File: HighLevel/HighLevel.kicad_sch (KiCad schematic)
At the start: 28 parts, among them J10 Conn_01x06, J4 USB_A, J5 CAN, J6 SERVO, J7 AUX, J8 SWD, J9 COMM, Q1 MOFSET_N, SW1 SW_SPDT, U6 NRF24L01_Breakout

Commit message: Final High Level + edits + footprint
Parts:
- added C1: 2.2u, Capacitor_SMD:C_0805_2012Metric, symbol Device:C_Small
- C2: renamed from C20; footprint (none) -> Capacitor_SMD:C_0805_2012Metric
- C3: renamed from C21; footprint (none) -> Capacitor_SMD:C_0805_2012Metric
- D2: renamed from D3; footprint (none) -> LED_SMD:LED_0805_2012Metric
- D3: renamed from D2; footprint (none) -> LED_SMD:LED_0805_2012Metric
- D4: renamed from D1; footprint (none) -> LED_SMD:LED_0805_2012Metric
- R1: renamed from R27; footprint (none) -> Resistor_SMD:R_0805_2012Metric
- R10: renamed from R15; footprint (none) -> Resistor_SMD:R_0805_2012Metric
- R11: renamed from R13; footprint (none) -> Resistor_SMD:R_0805_2012Metric
- R12: renamed from R14; footprint (none) -> Resistor_SMD:R_0805_2012Metric
- R2: renamed from R28; footprint (none) -> Resistor_SMD:R_0805_2012Metric
- R3: renamed from R29; footprint (none) -> Resistor_SMD:R_0805_2012Metric
- R4: renamed from R24; footprint (none) -> Resistor_SMD:R_0805_2012Metric
- R5: renamed from R25; footprint (none) -> Resistor_SMD:R_0805_2012Metric
- R6: renamed from R16; footprint (none) -> Resistor_SMD:R_0805_2012Metric
- R7: renamed from R20; footprint (none) -> Resistor_SMD:R_0805_2012Metric
- R8: renamed from R23; footprint (none) -> Resistor_SMD:R_0805_2012Metric
- R9: renamed from R26; footprint (none) -> Resistor_SMD:R_0805_2012Metric
- SW1: footprint (none) -> Resistor_SMD:R_0805_2012Metric
- renumbered D4 to D1, J4 to J1, J10 to J2, J9 to J3, J6 to J4, J8 to J6, U6 to U1
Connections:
- net GND: now also U1.1 (GND), C1.1
- net VCC: now also U1.2 (VCC)
- net mcu/HALL_3: now also R1.1
- net mcu/PC10_UART_TX: now also U1.7 (MISO)
- net mcu/PX11_UART_RX: now also U1.5 (SCK)
- net mcu/TX_SCK_MOSI: now also U1.6 (MOSI)
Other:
- sheet driver ports: added HI1, HI2, HI3, HO1, HO2, HO3, HS1, HS2, HS3, LI1, LI2, LI3, LO1, LO2, LO3, SENS_1, SENS_2, SENS_3, SENS_FILTER, SENS_SUPPLY; removed none
- sheet power ports: added GH_A, GH_B, GH_C, GL_A, GL_B, GL_C, SH_A, SH_B, SH_C; removed none
- moved on the sheet: U1

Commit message: Fix all errors
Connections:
- net VCC: now also C1.2
- net mcu/SPI3_CE: now reaches U1.3 (CE)
- net mcu/SPI3_CSN: now reaches U1.4 (~{CSN})
- net mcu/PC10_UART_TX renamed mcu/SPI3_MISO
- net mcu/PC12 renamed mcu/PC13
- net mcu/PX11_UART_RX renamed mcu/SPI3_SCK
- net mcu/TX_SCK_MOSI renamed mcu/SPI3_MOSI
- no-connect marks 0 -> 1
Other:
- sheet mcu ports: added PC13, SPI3_CE, SPI3_CSN, SPI3_MISO, SPI3_MOSI, SPI3_SCK; removed PC10_UART_TX, PC12, PX11_UART_RX, TX_SCK_MOSI
- moved on the sheet: D1, J7, Q1, R4

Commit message: Started PCB and added connections to MCU
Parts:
- J1: footprint (none) -> Connector_USB:USB_Micro-B_Molex-105017-0001
- J2: footprint (none) -> Connector_JST:JST_XH_B6B-XH-A_1x06_P2.50mm_Vertical
- J3: footprint (none) -> Connector_PinHeader_2.54mm:PinHeader_1x08_P2.54mm_Vertical
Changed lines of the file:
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@@
       (effects (font (size 1.27 1.27)))
     )
-    (property "Footprint" "" (at 106.68 88.9 0)
+    (property "Footprint" "Connector_PinHeader_2.54mm:PinHeader_1x08_P2.54mm_Vertical" (at 106.68 88.9 0)
       (effects (font (size 1.27 1.27)) hide)
     )
@@
       (effects (font (size 1.27 1.27)))
     )
-    (property "Footprint" "" (at 100.33 59.69 0)
+    (property "Footprint" "Connector_JST:JST_XH_B6B-XH-A_1x06_P2.50mm_Vertical" (at 100.33 59.69 0)
       (effects (font (size 1.27 1.27)) hide)
     )
@@
       (effects (font (size 1.27 1.27)))
     )
-    (property "Footprint" "" (at 83.82 35.56 0)
-      (effects (font (size 1.27 1.27)) hide)
-    )
+    (property "Footprint" "Connector_USB:USB_Micro-B_Molex-105017-0001" (at 83.82 35.56 0)
+      (effects (font (size 1.27 1.27)) hide)
+    )

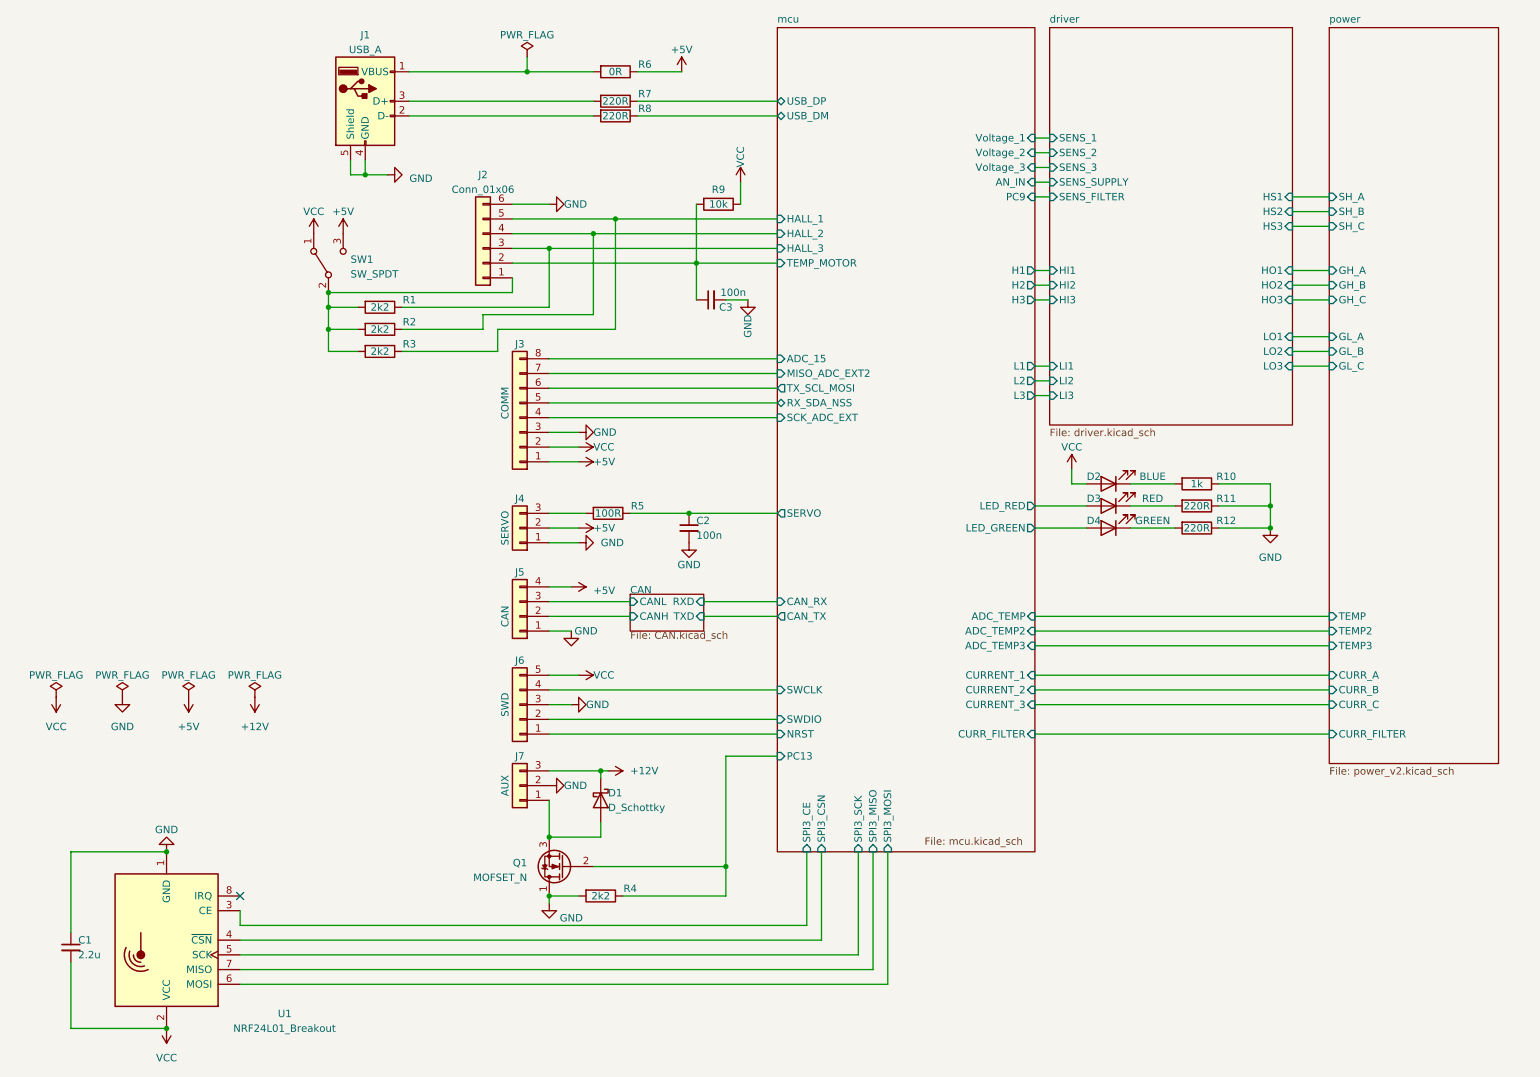
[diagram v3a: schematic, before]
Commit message: Added last two sheets and some footprints
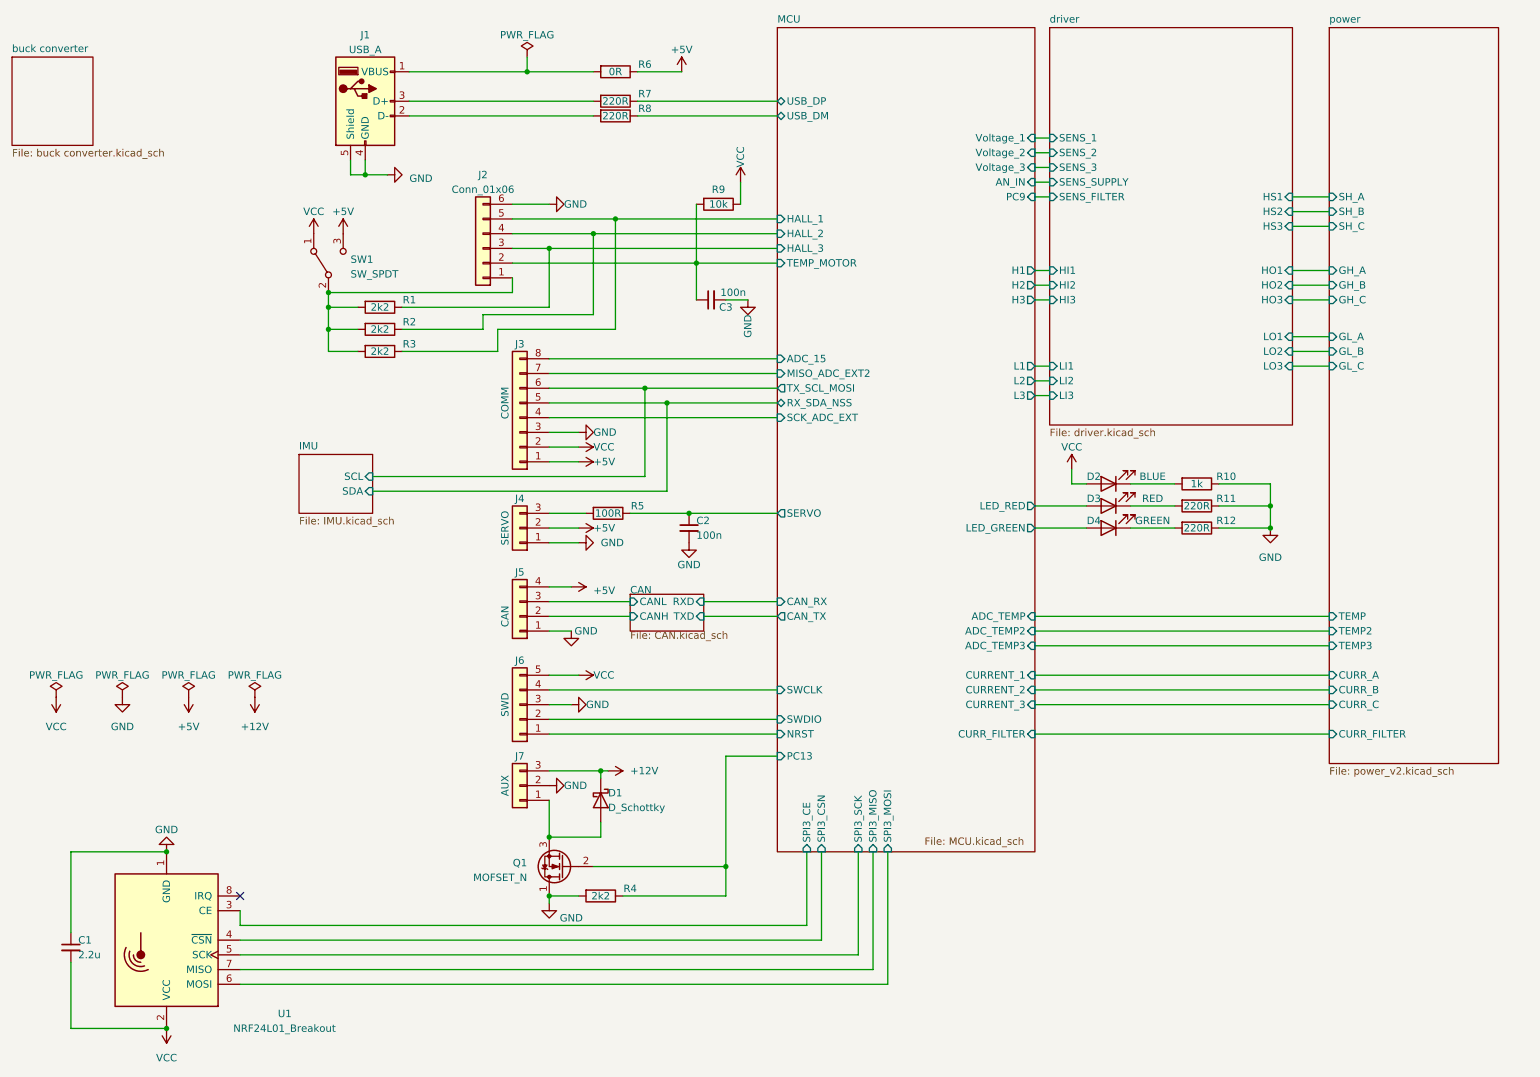
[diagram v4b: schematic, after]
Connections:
- net MCU/RX_SDA_NSS renamed IMU/SDA
- net MCU/TX_SCL_MOSI renamed IMU/SCL
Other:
- sheet mcu renamed MCU
- added sheet IMU (IMU.kicad_sch)
- added sheet buck converter (buck converter.kicad_sch)
- sheet MCU: file mcu.kicad_sch -> MCU.kicad_sch
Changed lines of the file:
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@@
   (junction (at 73.66 69.85) (diameter 0) (color 0 0 0 0)
+  )
+  (junction (at 132.08 86.36) (diameter 0) (color 0 0 0 0)
+  )
+  (junction (at 128.27 83.82) (diameter 0) (color 0 0 0 0)
   )
   (junction (at 137.16 62.23) (diameter 0) (color 0 0 0 0)
@@
     (stroke (width 0) (type default))
   )
-  (wire (pts (xy 111.76 83.82) (xy 151.13 83.82))
+  (wire (pts (xy 111.76 83.82) (xy 128.27 83.82))
     (stroke (width 0) (type default))
   )
@@
     (stroke (width 0) (type default))
   )
+  (wire (pts (xy 132.08 86.36) (xy 151.13 86.36))
+    (stroke (width 0) (type default))
+  )
   (wire (pts (xy 45.72 163.83) (xy 29.21 163.83))
     (stroke (width 0) (type default))
@@
     (stroke (width 0) (type default))
   )
+  (wire (pts (xy 81.28 101.6) (xy 132.08 101.6))
+    (stroke (width 0) (type default))
+  )
   (wire (pts (xy 123.19 73.66) (xy 123.19 54.61))
     (stroke (width 0) (type default))
@@
     (stroke (width 0) (type default))
   )
+  (wire (pts (xy 132.08 101.6) (xy 132.08 86.36))
+    (stroke (width 0) (type default))
+  )
   (wire (pts (xy 111.76 118.11) (xy 115.57 118.11))
     (stroke (width 0) (type default))
@@
     (stroke (width 0) (type default))
   )
+  (wire (pts (xy 81.28 99.06) (xy 128.27 99.06))
+    (stroke (width 0) (type default))
+  )
   (wire (pts (xy 116.84 93.98) (xy 111.76 93.98))
     (stroke (width 0) (type default))
@@
     (stroke (width 0) (type default))
   )
+  (wire (pts (xy 128.27 99.06) (xy 128.27 83.82))
+    (stroke (width 0) (type default))
+  )
   (wire (pts (xy 240.03 68.58) (xy 246.38 68.58))
     (stroke (width 0) (type default))
   )
+  (wire (pts (xy 128.27 83.82) (xy 151.13 83.82))
+    (stroke (width 0) (type default))
+  )
   (wire (pts (xy 111.76 149.86) (xy 120.65 149.86))
     (stroke (width 0) (type default))
@@
     (stroke (width 0) (type default))
   )
-  (wire (pts (xy 111.76 86.36) (xy 151.13 86.36))
+  (wire (pts (xy 111.76 86.36) (xy 132.08 86.36))
     (stroke (width 0) (type default))
   )
@@
     )
   )
+  (sheet (at 68.58 95.25) (size 12.7 10.16) (fields_autoplaced)
+    (stroke (width 0.1524) (type solid))
+    (fill (color 0 0 0 0.0000))
+    (property "Sheetname" "IMU" (at 68.58 94.5384 0)
+      (effects (font (size 1.27 1.27)) (justify left bottom))
+    )
+    (property "Sheetfile" "IMU.kicad_sch" (at 68.58 105.9946 0)
+      (effects (font (size 1.27 1.27)) (justify left top))
+    )
+    (pin "SCL" input (at 81.28 99.06 0)
+      (effects (font (size 1.27 1.27)) (justify right))
+    )
+    (pin "SDA" input (at 81.28 101.6 0)
+      (effects (font (size 1.27 1.27)) (justify right))
+    )
+    (instances
+      (project "HighLevel"
+        (path "/26149e3f-2822-4531-a73b-0a61b71078cc" (page "6"))
+      )
+    )
+  )
   (sheet (at 246.38 21.59) (size 29.21 127) (fields_autoplaced)
     (stroke (width 0.1524) (type solid))
@@
     )
   )
+  (sheet (at 19.05 26.67) (size 13.97 15.24) (fields_autoplaced)
+    (stroke (width 0.1524) (type solid))
+    (fill (color 0 0 0 0.0000))
+    (property "Sheetname" "buck converter" (at 19.05 25.9584 0)
+      (effects (font (size 1.27 1.27)) (justify left bottom))
+    )
+    (property "Sheetfile" "buck converter.kicad_sch" (at 19.05 42.4946 0)
+      (effects (font (size 1.27 1.27)) (justify left top))
+    )
+    (instances
+      (project "HighLevel"
+        (path "/26149e3f-2822-4531-a73b-0a61b71078cc" (page "7"))
+      )
+    )
+  )
   (sheet (at 151.13 21.59) (size 44.45 142.24)
     (stroke (width 0.1524) (type solid))
     (fill (color 0 0 0 0.0000))
-    (property "Sheetname" "mcu" (at 151.13 20.8784 0)
+    (property "Sheetname" "MCU" (at 151.13 20.8784 0)
       (effects (font (size 1.27 1.27)) (justify left bottom))
     )
-    (property "Sheetfile" "mcu.kicad_sch" (at 176.53 161.29 0)
+    (property "Sheetfile" "MCU.kicad_sch" (at 176.53 161.29 0)
       (effects (font (size 1.27 1.27)) (justify left top))
     )
